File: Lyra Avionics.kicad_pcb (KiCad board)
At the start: 4 copper layers, 62.1 x 62.1 mm, 58 parts, among them SW1 SW_Push, SW2 SW_Push, U1 RP2350_80QFN, U2 LSM6DSV16XTR, U3 W25Q128JVS, U4 SMA-KWE_C20415790, U5 GT-USB-7010ASV, U6 RA-01SH, U7 NCP1117-3.3_SOT223, U8 BME280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

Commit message: more updates
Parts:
- moved H2 13.5 mm to (87.0, 124.0)
- moved H4 6.95 mm to (112.0, 124.0)
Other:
- board text added: "LYRA"

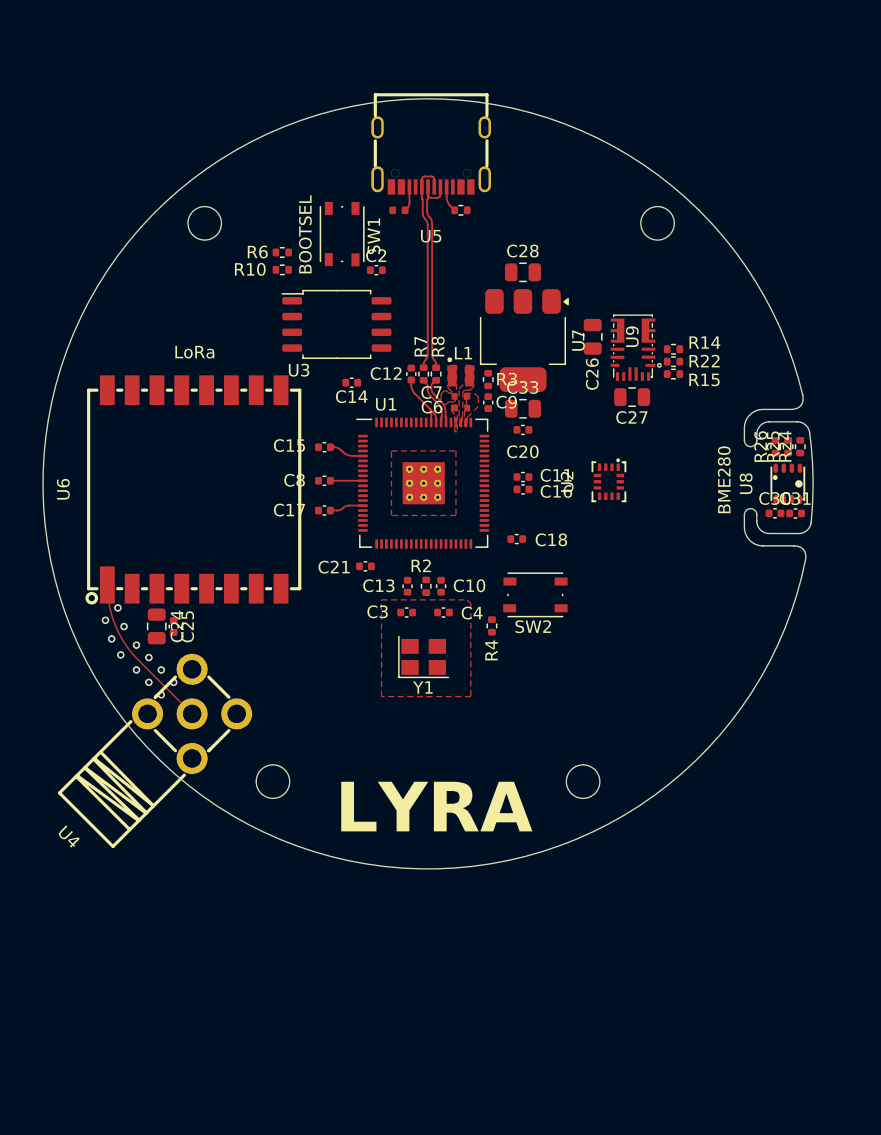
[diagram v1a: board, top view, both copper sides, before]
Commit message: Completed first revision of PCB
Fully routed and checked in tolerance with JLCPCB manufacturing capabilities for 4L boards. Schematic needs checking and LCSC parts need assigning.
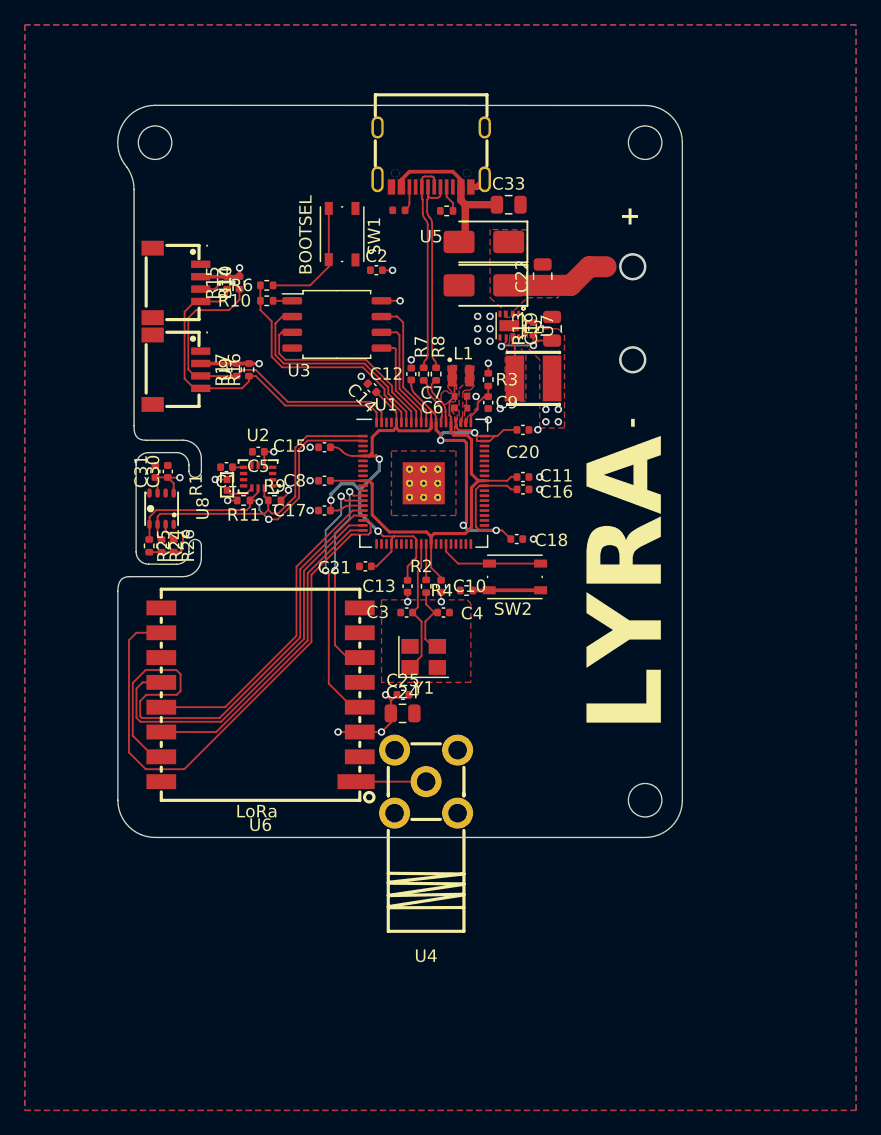
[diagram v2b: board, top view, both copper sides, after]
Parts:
- removed C26, C27: 22u, Capacitor_SMD:C_0805_2012Metric
- removed C28: 10u, Capacitor_SMD:C_0805_2012Metric
- removed H4: MountingHole, MountingHole:MountingHole_2.7mm_M2.5
- removed R22: 24k, Resistor_SMD:R_0402_1005Metric
- added C1: 100n, Capacitor_SMD:C_0402_1005Metric, F.Cu at (83.3, 98.7)
- added C19: 22u, Capacitor_SMD:C_0805_2012Metric, F.Cu at (109.5, 87.5)
- added C22: 22u, Capacitor_SMD:C_0805_2012Metric, F.Cu at (108.7, 83.3)
- added C5: 100n, Capacitor_SMD:C_0402_1005Metric, F.Cu at (85.8, 97.4)
- added D1: SS34, PCM_JLCPCB:D_SMA, F.Cu at (104.0, 80.5)
- added D2: SS34, PCM_JLCPCB:D_SMA, F.Cu at (104.0, 84.0)
- added L2: PA4332_222NLT, footprint:IND-SMD_L4.2-W4.2_PA4332, F.Cu at (108.0, 91.5)
- added R1: 10k, footprint:R0402, F.Cu at (83.3, 100.1)
- added R11: 4.7k, Resistor_SMD:R_0402_1005Metric, F.Cu at (84.6, 101.3)
- added R13: 100k, Resistor_SMD:R_0402_1005Metric, F.Cu at (108.0, 87.5)
- added R16: 4.7k, Resistor_SMD:R_0402_1005Metric, F.Cu at (85.1, 90.8)
- added R17: 4.7k, Resistor_SMD:R_0402_1005Metric, F.Cu at (84.1, 90.8)
- added R9: 4.7k, Resistor_SMD:R_0402_1005Metric, F.Cu at (87.1, 101.3)
- added U10: QWIIC/Stemma I2C, footprint:CONN-SMD_4P-P1.00_SM04B-SRSS-TB-LF-SN, F.Cu at (79.2, 83.8)
- R14, R15: value 75k -> 4.7k
- U7: value NCP1117-3.3_SOT223 -> TPS62162DSG; footprint Package_TO_SOT_SMD:SOT-223-3_TabPin2 -> footprint:WSON-8_L2.0-W2.0-P0.50-TL-EP
- U9: value MPM3610AGQV-Z -> QWIIC/Stemma I2C; footprint footprint:QFN-20_L5.0-W3.0-P0.50-TL_MPM3610AGQV -> footprint:CONN-SMD_4P-P1.00_SM04B-SRSS-TB-LF-SN
- moved R25 52.1 mm to (77.0, 105.0), turned to -90 degrees
- moved R24 52.1 mm to (78.0, 105.0), turned to -90 degrees
- moved C31 51.7 mm to (77.5, 99.0), turned to 90 degrees
- moved U8 50.5 mm to (78.0, 102.0), turned to -90 degrees
- moved R26 49.2 mm to (79.0, 105.0), turned to -90 degrees
- moved C30 49.1 mm to (78.5, 99.0), turned to 90 degrees
- moved U9 36.8 mm to (79.2, 90.8), turned to -90 degrees
- moved R15 36.7 mm to (83.3, 83.8), turned to 90 degrees
- moved R14 35.4 mm to (84.3, 83.8), turned to 90 degrees
- moved H2 30.0 mm to (117.0, 125.5)
- moved U2 28.3 mm to (85.8, 99.4), turned to 0 degrees
- moved C24 21.0 mm to (97.5, 118.5), turned to 0 degrees
- moved U4 19.6 mm to (99.3, 124.0), turned to 180 degrees
- moved C25 19.3 mm to (97.5, 117.0), turned to 0 degrees
- moved U6 17.4 mm to (86.0, 117.0), turned to 180 degrees
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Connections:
- R14 pad 1: Net-(U9-FB) -> /GPIO2
- R15 pad 1: Net-(U9-EN) -> /GPIO3
- R15 pad 2: VBAT -> +3V3
- U2 pad 12: unconnected-(U2-CS-Pad12) -> Net-(U2-CS)
- U2 pad 13: unconnected-(U2-SCL-Pad13) -> /GPIO5
- U2 pad 14: unconnected-(U2-SDA-Pad14) -> /GPIO4
- U2 pad 5: unconnected-(U2-Vdd_IO-Pad5) -> +3V3
- U2 pad 6: unconnected-(U2-GND-Pad6) -> GND
- U2 pad 7: unconnected-(U2-GND-Pad7) -> GND
- U2 pad 8: unconnected-(U2-Vdd-Pad8) -> +3V3
- U6 pad 10: unconnected-(U6-BUSY-Pad10) -> /GPIO18
- U6 pad 12: unconnected-(U6-SCK-Pad12) -> /GPIO19
- U6 pad 13: unconnected-(U6-MISO-Pad13) -> /GPIO16
- U6 pad 14: unconnected-(U6-MOSI-Pad14) -> /GPIO20
- U6 pad 15: unconnected-(U6-NSS-Pad15) -> /GPIO17
- U6 pad 4: unconnected-(U6-RESET-Pad4) -> /GPIO15
- U6 pad 6: unconnected-(U6-DIO1-Pad6) -> /GPIO14
- U7 pad 2: +3V3 -> Net-(U7-EN)
- U7 pad 3: VBUS -> Net-(U7-EN)
- U9 pad 1: Net-(U9-FB) -> GND
- U9 pad 2: unconnected-(U9-VCC-Pad2) -> +3V3
- U9 pad 3: GND -> /GPIO2
- U9 pad 4: /SW -> /GPIO3
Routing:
- net +3V3: track 11.2 -> 120.5 mm, vias 0 -> 27
- net /GPIO17: track 0.00 -> 45.9 mm
- net /GPIO18: track 0.00 -> 44.5 mm
- net +1V1: track 2.62 -> 36.8 mm
- net /GPIO19: track 0.00 -> 32.7 mm
- net /GPIO2: track 0.00 -> 31.5 mm
- net /GPIO3: track 0.00 -> 28.5 mm
- net /GPIO5: track 0.00 -> 27.1 mm, vias 0 -> 2
- net /GPIO20: track 0.00 -> 26.2 mm
- net /GPIO16: track 0.00 -> 26.1 mm
- net /GPIO4: track 0.00 -> 25.7 mm
- net /GPIO15: track 0.00 -> 20.9 mm, vias 0 -> 2
- net /QSPI_SS: track 0.00 -> 19.6 mm
- net /QSPI_SD1: track 0.00 -> 17.7 mm
- net /GPIO14: track 0.00 -> 16.5 mm, vias 0 -> 2
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- added copper zone on In2.Cu, net +3V3
- added copper zone on B.Cu, net GND
- added copper zone on F.Cu, net Net-(U7-EN)
- added copper zone on F.Cu, net Net-(U7-SW)
- removed copper zone on In2.Cu, net GND
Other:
- board size 62.1 x 62.1 mm -> 45.5 x 59 mm
- board text added: "+"
- board text added: "-"

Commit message: Added local library
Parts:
- C1, C10, C11, C12, C13, C14, C15, C16, C17, C18, C2, C20, C21, C25, C3, C30, C31, C4, C5, C8, C9: footprint Capacitor_SMD:C_0402_1005Metric -> Library:C_0402_1005Metric
- C19, C22, C24, C33: footprint Capacitor_SMD:C_0805_2012Metric -> Library:C_0805_2012Metric
- C6, C7: footprint RP2350_80QFN_minimal:C_0402_1005Metric_small_pads -> Library:C_0402_1005Metric_small_pads
- D1, D2: footprint PCM_JLCPCB:D_SMA -> Library:D_SMA
- H1, H2, H3: footprint MountingHole:MountingHole_2.7mm_M2.5 -> Library:MountingHole_2.7mm_M2.5
- L1: footprint RP2350_80QFN_minimal:L_pol_2016 -> Library:L_pol_2016
- L2: footprint footprint:IND-SMD_L4.2-W4.2_PA4332 -> Library:IND-SMD_L4.2-W4.2_PA4332
- R1: footprint footprint:R0402 -> Library:R0402
- R10, R11, R13, R14, R15, R16, R17, R2, R24, R25, R26, R3, R4, R6, R7, R8, R9: footprint Resistor_SMD:R_0402_1005Metric -> Library:R_0402_1005Metric
- R12: footprint PCM_SparkFun-Resistor:R_0402_1005Metric -> Library:R_0402_1005Metric
- R5: footprint PCM_JLCPCB:R_0402 -> Library:R_0402
- SW1, SW2: footprint Button_Switch_SMD:SW_Push_1P1T_NO_Vertical_Wuerth_434133025816 -> Library:SW_Push_1P1T_NO_Vertical_Wuerth_434133025816
- U1: footprint RP2350_80QFN_minimal:RP2350-QFN-80-1EP_10x10_P0.4mm_EP3.4x3.4mm_ThermalVias -> Library:RP2350-QFN-80-1EP_10x10_P0.4mm_EP3.4x3.4mm_ThermalVias
- U10, U9: footprint footprint:CONN-SMD_4P-P1.00_SM04B-SRSS-TB-LF-SN -> Library:CONN-SMD_4P-P1.00_SM04B-SRSS-TB-LF-SN
- U2: footprint footprint:LGA-14_L3.0-W2.5-P0.50-BR -> Library:LGA-14_L3.0-W2.5-P0.50-BR
- U3: footprint Package_SO:SOIC-8_5.23x5.23mm_P1.27mm -> Library:SOIC-8_5.23x5.23mm_P1.27mm
- U4: footprint footprint:SMA-TH_SMA-KWE -> Library:SMA-TH_SMA-KWE
- U5: footprint easyeda2kicad:USB-C-SMD_G-SWITCH_GT-USB-7010ASV -> Library:USB-C-SMD_G-SWITCH_GT-USB-7010ASV
- U6: footprint footprint:WIRELM-SMD_RA-01SH -> Library:WIRELM-SMD_RA-01SH
- U7: footprint footprint:WSON-8_L2.0-W2.0-P0.50-TL-EP -> Library:WSON-8_L2.0-W2.0-P0.50-TL-EP
- U8: footprint footprint:LGA-8_BME280_BL -> Library:LGA-8_BME280_BL
- Y1: footprint Crystal:Crystal_SMD_3225-4Pin_3.2x2.5mm -> Library:Crystal_SMD_3225-4Pin_3.2x2.5mm

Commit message: Initial minor fixes of routing
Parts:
- added CN1: S2B-PH-SM4-TB(LF)(SN), Connectors:CONN-SMD_P2.00_S2B-PH-SM4-TB-LF-SN, F.Cu at (114.9, 79.8)
- C6, C7: footprint Library:C_0402_1005Metric_small_pads -> RP2350_80QFN_minimal:C_0402_1005Metric_small_pads
- L1: footprint Library:L_pol_2016 -> RP2350_80QFN_minimal:L_pol_2016
- U1: footprint Library:RP2350-QFN-80-1EP_10x10_P0.4mm_EP3.4x3.4mm_ThermalVias -> RP2350_80QFN_minimal:RP2350-QFN-80-1EP_10x10_P0.4mm_EP3.4x3.4mm_ThermalVias
- moved C22 6.25 mm to (102.5, 84.0), turned to 180 degrees
- moved D2 4.05 mm to (108.0, 84.0), turned to 0 degrees
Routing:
- net /GPIO17: track 45.9 -> 29.2 mm, vias 0 -> 2
- net Net-(U7-EN): track 8.47 -> 2.56 mm
- net VBAT: track 0.00 -> 4.84 mm
- net GND: vias 20 -> 21
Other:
- outline, holes or cut-outs redrawn

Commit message: Fix
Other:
- board text added: "by Azlan (mas338)"
